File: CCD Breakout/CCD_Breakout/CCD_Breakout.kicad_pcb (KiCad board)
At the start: 2 copper layers, 16 x 76.5 mm, 11 parts, among them Q1 PNP, U1 ILX511

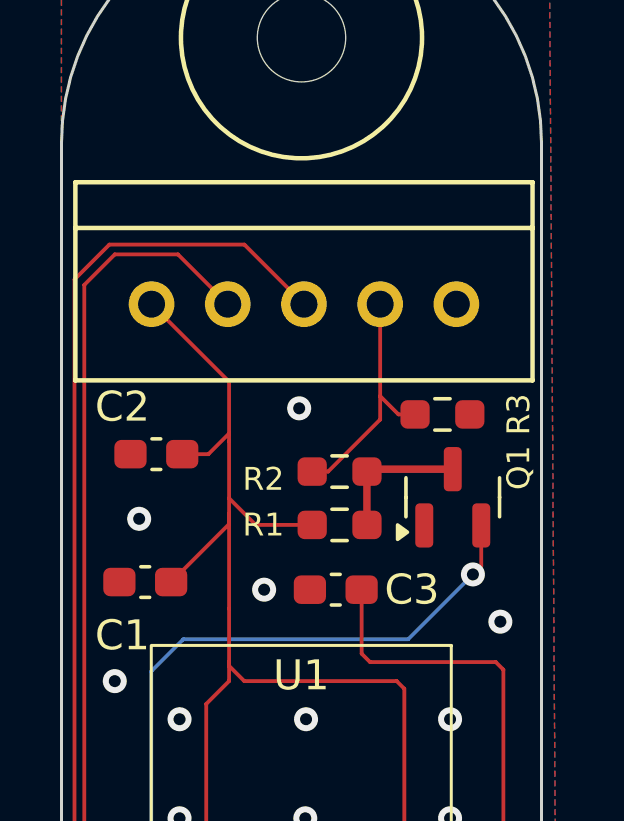
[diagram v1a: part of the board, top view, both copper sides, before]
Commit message: Fixed bjt and SL on CCD Breakout
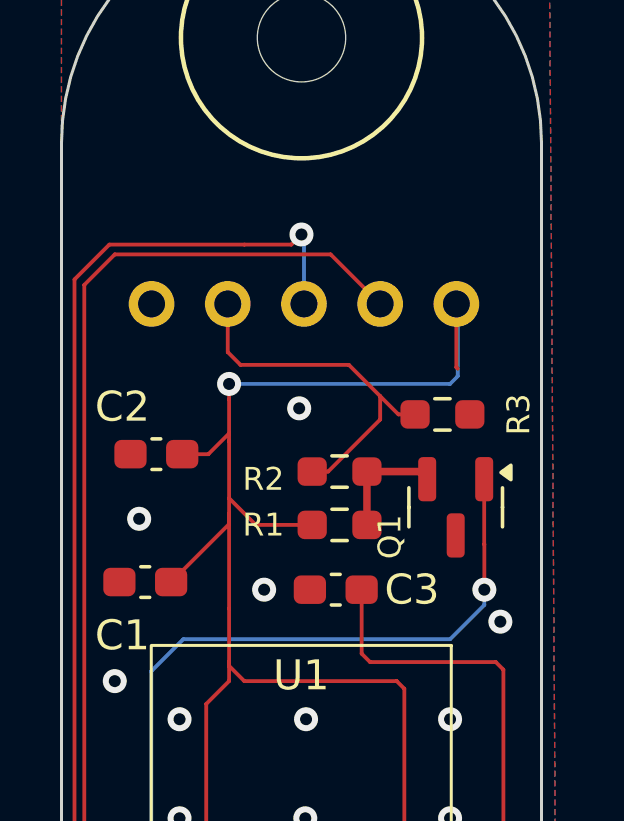
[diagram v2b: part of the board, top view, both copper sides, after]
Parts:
- Conn1: moved to B.Cu
- moved Conn1 10.2 mm to (76.4, 41.5), turned to 180 degrees
- moved Q1 0.35 mm to (76.4, 48.3), turned to -90 degrees
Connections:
- Q1 pad 1: GND -> Net-(Q1-B)
- Q1 pad 2: Net-(Q1-B) -> Net-(Q1-E)
- Q1 pad 3: Net-(Q1-E) -> GND
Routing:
- net +5V: track 91.5 -> 100.1 mm, vias 0 -> 1
- net CLK: track 37.1 -> 42.2 mm
- net Vout: track 8.25 -> 12.5 mm
- net Net-(Q1-B): track 21.0 -> 23.4 mm
- net ROG: track 55.7 -> 57.3 mm, vias 0 -> 1
- net Net-(Q1-E): track 4.67 -> 4.00 mm
